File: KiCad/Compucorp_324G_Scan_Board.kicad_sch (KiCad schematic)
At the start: 13 parts, among them J1 Panaplex, J2 Power In, U1 BR 16252

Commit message: Updated keyboard schematic
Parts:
- added J4: From Keyboard, symbol Connector_Generic:Conn_01x28
- J1: value Panaplex -> BR 16252
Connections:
- net A_{10} is gone; now on net Digit_{10}: J1.18 (Pin_18)
- net A_{11} is gone; now on net Digit_{11}: J1.16 (Pin_16)
- net A_{12} is gone; now on net Digit_{12}: J1.14 (Pin_14)
- net A_{13} is gone; now on net Digit_{13}: J1.12 (Pin_12), R14.1, R9.1
- net A_{14} is gone; now on net Digit_{14}: J1.10 (Pin_10)
- net A_{15} is gone; now on net Digit_{15}: J1.4 (Pin_4)
- net A_{16} is gone; now on net Digit_{16}: J1.2 (Pin_2)
- net A_{1} is gone; now on net Digit_{1}: J1.39 (Pin_39)
- net A_{2} is gone; now on net Digit_{2}: J1.37 (Pin_37)
- net A_{3} is gone; now on net Digit_{3}: J1.35 (Pin_35)
- net A_{4} is gone; now on net Digit_{4}: J1.25 (Pin_25)
- net A_{5} is gone; now on net Digit_{5}: J1.24 (Pin_24)
- net A_{6} is gone; now on net Digit_{6}: J1.23 (Pin_23)
- net A_{7} is gone; now on net Digit_{7}: J1.21 (Pin_21)
- net A_{8} is gone; now on net Digit_{8}: J1.20 (Pin_20)
- net A_{9} is gone; now on net Digit_{9}: J1.19 (Pin_19)
- net K_{a}: now also U1.1 (Cathode_{a})
- net K_{b}: now also U1.3 (Cathode_{b})
- net K_{c}: now also U1.5 (Cathode_{c})
- net K_{d}: now also U1.27 (Cathode_{d})
- net K_{e}: now also U1.29 (Cathode_{e})
- net K_{f}: now also U1.33 (Cathode_{f})
- net K_{g}: now also U1.31 (Cathode_{g})
- net K_{h}: now also U1.7 (Cathode_{h})
- net K_{i}: now also U1.11 (Cathode_{j}), U1.9 (Cathode_{i})
- net Digit_{12}: now reaches U1.10 (Anode_{12})
- net Digit_{11}: now reaches U1.12 (Anode_{11})
- net Digit_{10}: now reaches U1.14 (Anode_{10})
- net Digit_{9}: now reaches U1.16 (Anode_{9})
- net Digit_{8}: now reaches U1.18 (Anode_{8})
- net Digit_{16}: now reaches U1.2 (Anode_{16})
- net Digit_{7}: now reaches U1.20 (Anode_{7})
- net Digit_{6}: now reaches U1.22 (Anode_{6})
- net Digit_{5}: now reaches U1.24 (Anode_{5})
- net Digit_{4}: now reaches U1.26 (Anode_{4})
- net Digit_{3}: now reaches U1.28 (Anode_{3})
- net Digit_{2}: now reaches U1.30 (Anode_{2})
- net Digit_{1}: now reaches U1.32 (Anode_{1})
- net Digit_{15}: now reaches U1.4 (Anode_{15})
- net Digit_{14}: now reaches U1.6 (Anode_{14})
- net Digit_{13}: now reaches U1.8 (Anode_{13})
- new net KB Col 1: J4.7 (Pin_7)
- new net KB Col 2: J4.12 (Pin_12)
- new net KB Col 3: J4.8 (Pin_8)
- new net KB Col 4: J4.11 (Pin_11)
- new net KB Col 5: J4.9 (Pin_9)
- new net KB Col 6: J4.13 (Pin_13)
- new net KB Col 7: J4.16 (Pin_16)
- new net KB Col 8: J4.17 (Pin_17)
- new net KB Col 9: J4.18 (Pin_18)
- new net KB FED: J4.21 (Pin_21)
- new net KB GRAD: J4.24 (Pin_24)
- new net KB LOAD: J4.22 (Pin_22)
- new net KB PROG 1: J4.6 (Pin_6)
- new net KB RUN: J4.23 (Pin_23), J4.5 (Pin_5)
- new net KB Row 1: J4.1 (Pin_1)
- new net KB Row 2: J4.2 (Pin_2)
- new net KB Row 3: J4.3 (Pin_3)
- new net KB Row 4: J4.4 (Pin_4)
- new net KB Row 5: J4.25 (Pin_25)
- new net KB Row 6: J4.26 (Pin_26)
- new net KB Row 7: J4.27 (Pin_27)
- new net KB Row 8: J4.28 (Pin_28)
- new net TCL02 Pin 38: J4.20 (Pin_20)
- no-connect marks 14 -> 18
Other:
- moved on the sheet: J1, R10, R7, R8, R9, U1

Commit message: Update Compucorp_324G_Scan_Board.kicad_sch
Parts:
- added D1, D2, D3, D4, D5, D6, D7, D8: D, symbol Device:D
- added U4: TMC 1869, symbol Clueless_Engineer:TMC_1869
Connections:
- net KB Col 7: now also U4.33 (Pin_33)
- net KB Col 8: now also U4.34 (Pin_34)
- net KB Col 9: now also U4.35 (Pin_35)
- net KB FED: now also D1.2 (A)
- net KB GRAD: now also D5.2 (A)
- net KB LOAD: now also D3.2 (A)
- net KB Row 5: now also D2.2 (A)
- net KB Row 6: now also D4.2 (A)
- net KB Row 8: now also D8.2 (A)
- net TCL02 Pin 38: now also U4.38 (Pin_38)
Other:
- moved on the sheet: U2, U3

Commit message: Updates to schematic
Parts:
- removed J1: BR 16252, symbol Connector_Generic:Conn_01x40
- removed U1: BR 16252, symbol Clueless_Engineer:Panaplex II 16dig
- removed U2, U3: ~, symbol Clueless_Engineer:UHP480
- removed U4: TMC 1869, symbol Clueless_Engineer:TMC_1869
- added J1: Scan Interboard, symbol Connector_Generic:Conn_02x40_Row_Letter_First
- added U1: BR 16252, symbol Compucorp_324G_Scientist:Panaplex II 16dig
- added U2, U3: UHP480, symbol Compucorp_324G_Scientist:UHP480
- added U4: TMC 1869, symbol Compucorp_324G_Scientist:TMC_1869
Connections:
- net Digit_{10}: now also J1.a18 (Pin_a18), U1.14 (Anode_{10})
- net Digit_{11}: now also J1.a16 (Pin_a16), U1.12 (Anode_{11})
- net Digit_{12}: now also J1.a14 (Pin_a14), U1.10 (Anode_{12})
- net Digit_{13}: now also J1.a12 (Pin_a12), U1.8 (Anode_{13})
- net Digit_{14}: now also J1.a10 (Pin_a10), U1.6 (Anode_{14})
- net Digit_{15}: now also J1.a4 (Pin_a4), U1.4 (Anode_{15})
- net Digit_{16}: now also J1.a2 (Pin_a2), U1.2 (Anode_{16})
- net Digit_{1}: now also J1.a39 (Pin_a39), U1.32 (Anode_{1})
- net Digit_{2}: now also J1.a37 (Pin_a37), U1.30 (Anode_{2})
- net Digit_{3}: now also J1.a35 (Pin_a35), U1.28 (Anode_{3})
- net Digit_{4}: now also J1.a25 (Pin_a25), U1.26 (Anode_{4})
- net Digit_{5}: now also J1.a24 (Pin_a24), U1.24 (Anode_{5})
- net Digit_{6}: now also J1.a23 (Pin_a23), U1.22 (Anode_{6})
- net Digit_{7}: now also J1.a21 (Pin_a21), U1.20 (Anode_{7})
- net Digit_{8}: now also J1.a20 (Pin_a20), U1.18 (Anode_{8})
- net Digit_{9}: now also J1.a19 (Pin_a19), U1.16 (Anode_{9})
- net KB Col 7: now also U4.33 (Pin_33)
- net KB Col 8: now also U4.34 (Pin_34)
- net KB Col 9: now also U4.35 (Pin_35)
- net K_{a}: now also J1.a1 (Pin_a1), U1.1 (Cathode_{a})
- net K_{b}: now also J1.a3 (Pin_a3), U1.3 (Cathode_{b})
- net K_{c}: now also J1.a9 (Pin_a9), U1.5 (Cathode_{c})
- net K_{d}: now also J1.a26 (Pin_a26), U1.27 (Cathode_{d})
- net K_{e}: now also J1.a36 (Pin_a36), U1.29 (Cathode_{e})
- net K_{f}: now also J1.a40 (Pin_a40), U1.33 (Cathode_{f})
- net K_{g}: now also J1.a38 (Pin_a38), U1.31 (Cathode_{g})
- net K_{h}: now also J1.a11 (Pin_a11), U1.7 (Cathode_{h})
- net K_{i}: now also J1.a13 (Pin_a13), J1.a15 (Pin_a15), U1.11 (Cathode_{j}), U1.9 (Cathode_{i})
- net U2_Pin9: now also U2.9 (Pin9)
- net U3_Pin9: now also U3.9 (Pin9)
- net TCL02 Pin 38 renamed TCL02_38
- net TCL02_38: now also U4.38 (Pin_38)

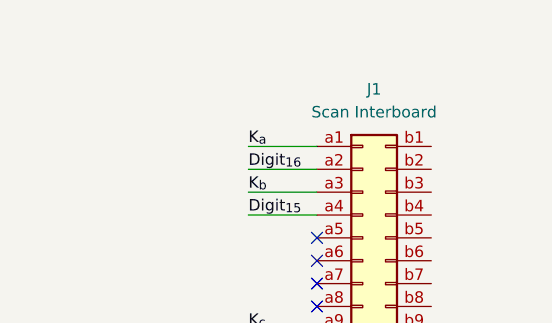
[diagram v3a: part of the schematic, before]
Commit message: Started on other board schematics
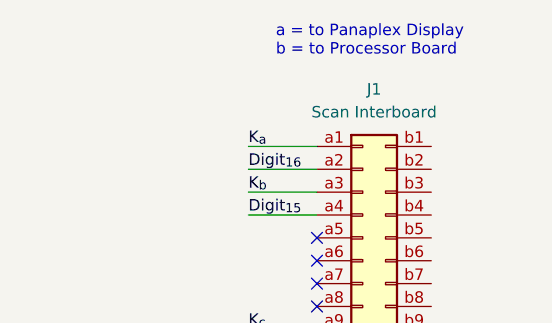
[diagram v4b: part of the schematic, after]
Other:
- note added: "a = to Panaplex Display b = to Processor Board"
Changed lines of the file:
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@@
 		(company "Brett Hallen")
+	)
+	(text "a = to Panaplex Display\nb = to Processor Board"
+		(exclude_from_sim no)
+		(at 246.888 23.876 0)
+		(effects
+			(font
+				(size 1.27 1.27)
+			)
+			(justify left)
+		)
 	)
 	(junction

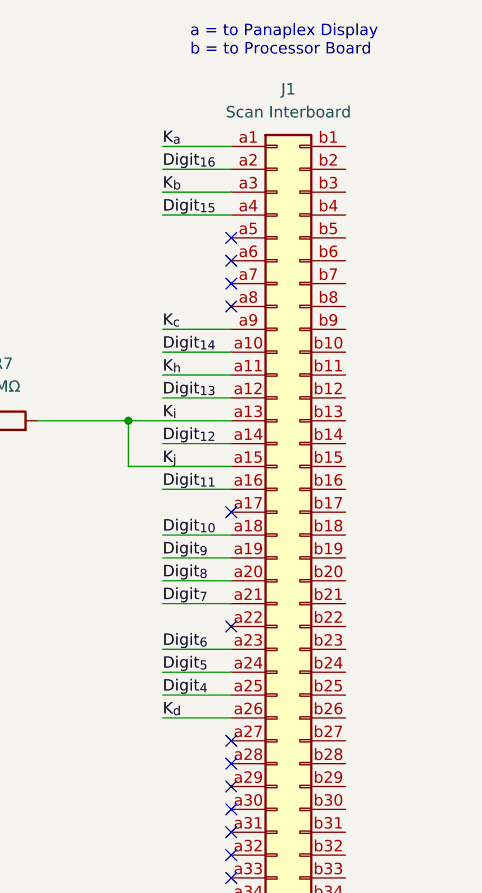
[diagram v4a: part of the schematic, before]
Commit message: Started Memory Board schematic
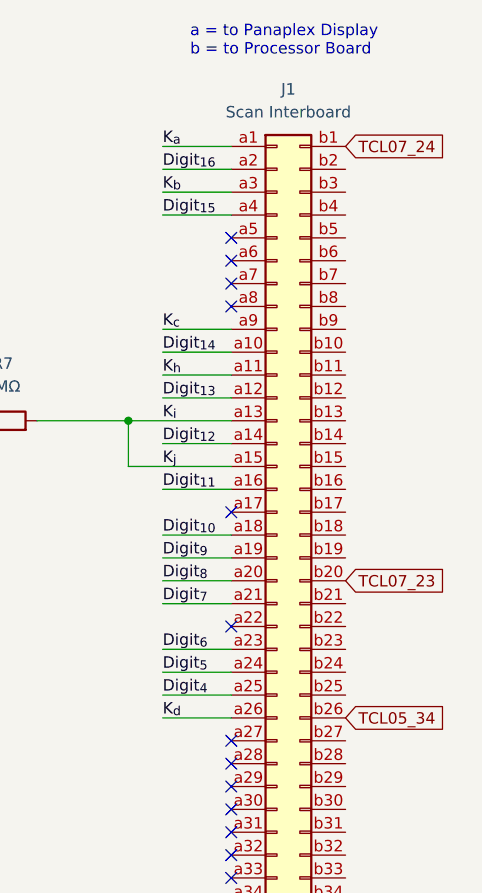
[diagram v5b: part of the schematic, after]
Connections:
- net TCL07_24: now reaches J1.b1 (Pin_b1)
- net TCL07_23: now reaches J1.b20 (Pin_b20)
- net TCL05_34: now reaches J1.b26 (Pin_b26)
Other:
- title: Compucorp 320-Series Scan Board -> Compucorp 300-Series Scan Board
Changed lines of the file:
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@@
 	(generator "eeschema")
 	(generator_version "9.0")
-	(paper "A4")
+	(paper "A3")
 	(title_block
-		(title "Compucorp 320-Series Scan Board")
+		(title "Compucorp 300-Series Scan Board")
 		(rev "WIP")
 		(company "Brett Hallen")
@@
 		)
 	)
+	(global_label "TCL07_23"
+		(shape input)
+		(at 264.16 83.82 0)
+		(fields_autoplaced yes)
+		(effects
+			(font
+				(size 1.27 1.27)
+			)
+			(justify left)
+		)
+		(property "Intersheetrefs" "${INTERSHEET_REFS}"
+			(at 276.2165 83.82 0)
+			(effects
+				(font
+					(size 1.27 1.27)
+				)
+				(justify left)
+				(hide yes)
+			)
+		)
+	)
 	(global_label "KB LOAD"
 		(shape input)
@@
 		)
 	)
+	(global_label "TCL05_34"
+		(shape input)
+		(at 264.16 99.06 0)
+		(fields_autoplaced yes)
+		(effects
+			(font
+				(size 1.27 1.27)
+			)
+			(justify left)
+		)
+		(property "Intersheetrefs" "${INTERSHEET_REFS}"
+			(at 276.2165 99.06 0)
+			(effects
+				(font
+					(size 1.27 1.27)
+				)
+				(justify left)
+				(hide yes)
+			)
+		)
+	)
 	(global_label "KB RUN"
 		(shape input)
@@
 				(hide yes)
 			)
+		)
+	)
+	(global_label "TCL07_24"
+		(shape input)
+		(at 264.16 35.56 0)
+		(fields_autoplaced yes)
+		(effects
+			(font
+				(size 1.27 1.27)
+			)
+			(justify left)
+		)
+		(property "Intersheetrefs" "${INTERSHEET_REFS}"
+			(at 276.2165 35.56 0)
+			(effects
+				(font
+					(size 1.27 1.27)
+				)
+				(justify left)
+				(hide yes)
+			)

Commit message: Memory board updates
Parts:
- removed U4: TMC 1869, symbol Compucorp_324G_Scientist:TMC_1869
- added U4: TMC1869 (TCL02), symbol Compucorp_324G_Scientist:TMC1869
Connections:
- net KB Col 7: now also U4.33 (Pin_33)
- net KB Col 8: now also U4.34 (Pin_34)
- net KB Col 9: now also U4.35 (Pin_35)
- net TCL02_38: now also U4.38 (Pin_38)

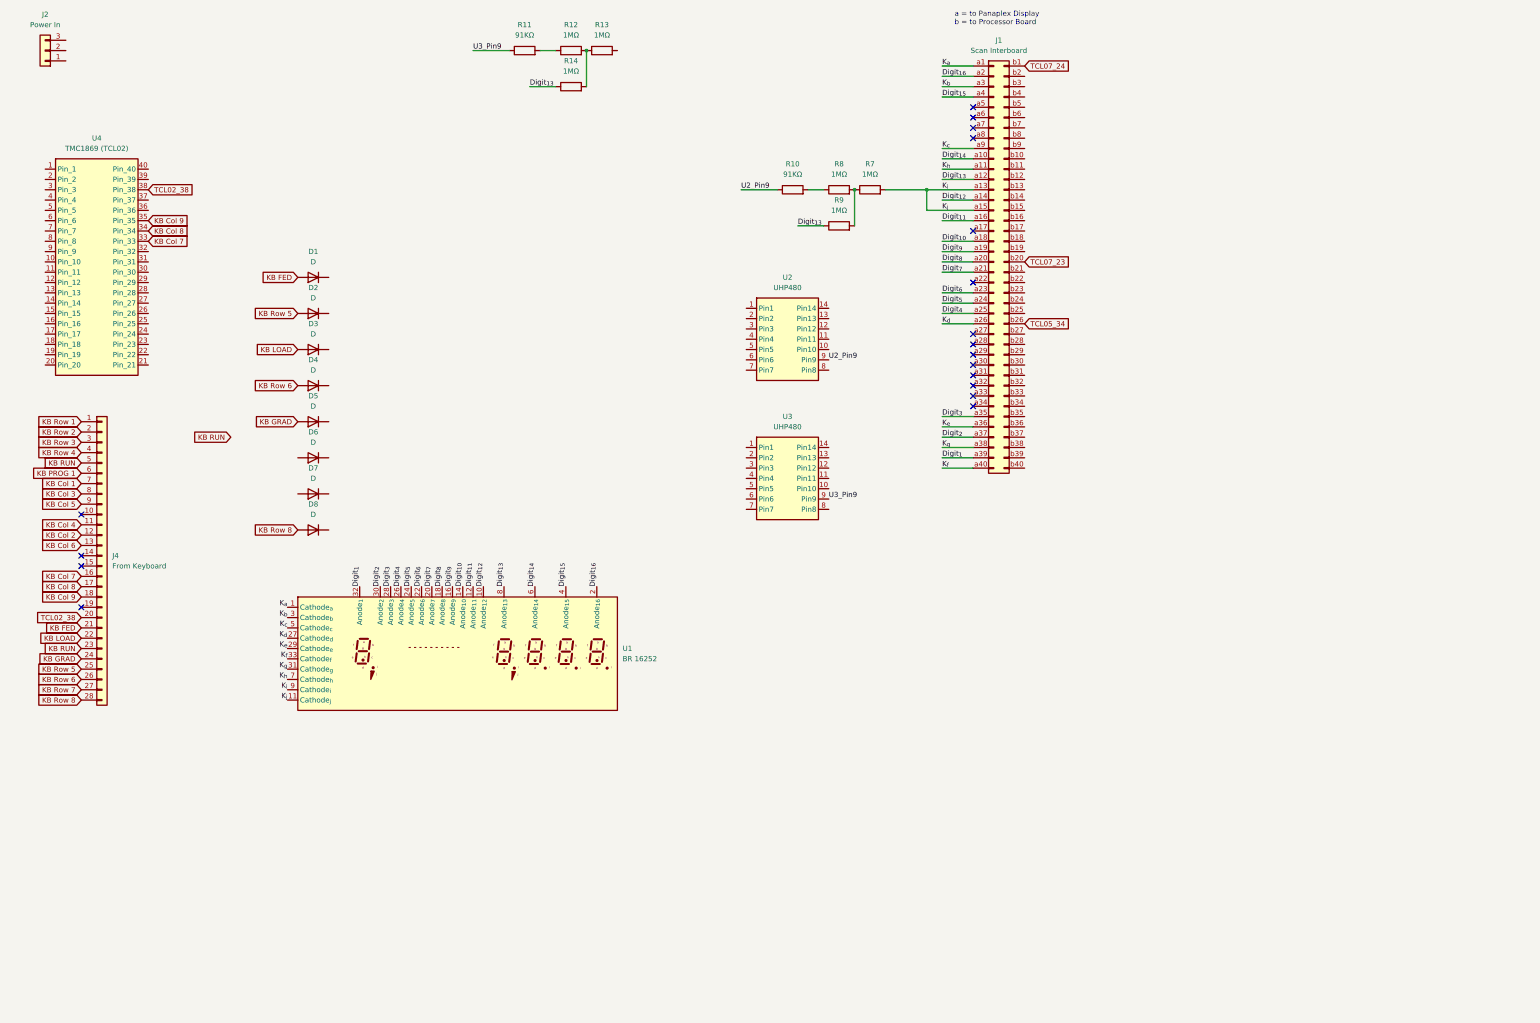
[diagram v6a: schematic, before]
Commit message: Schematic updates
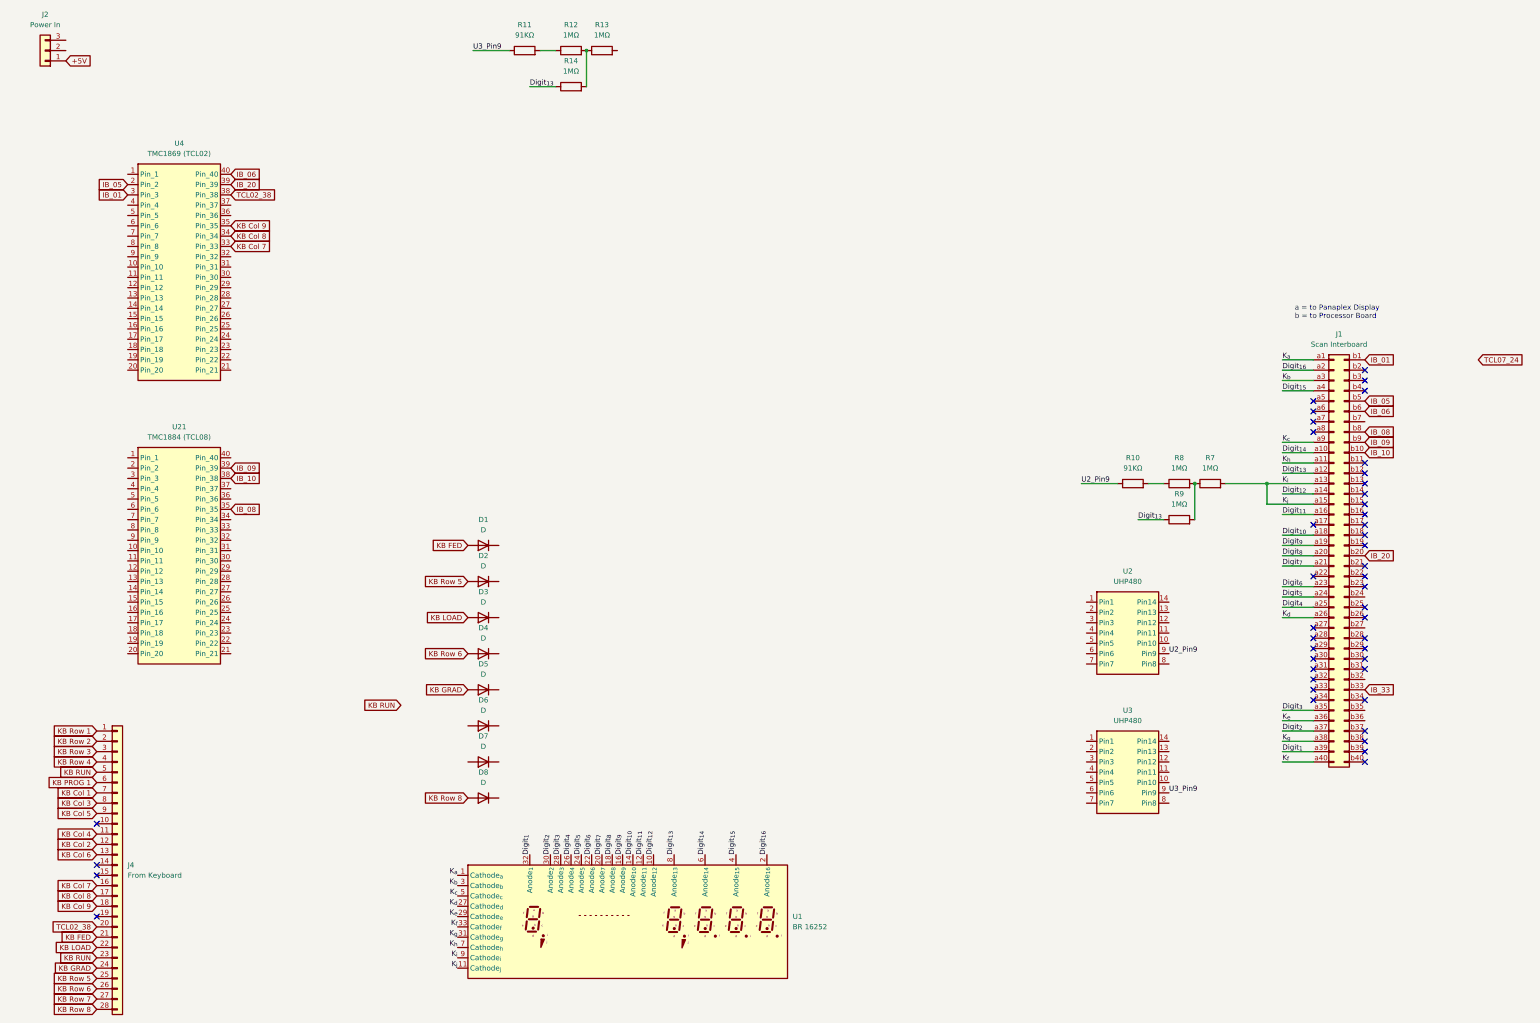
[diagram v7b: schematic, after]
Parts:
- added U21: TMC1884 (TCL08), symbol Compucorp_324G_Scientist:TMC1884
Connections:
- net TCL07_23 is gone; now on net IB_20: J1.b20 (Pin_b20)
- net TCL07_24: no longer J1.b1 (Pin_b1)
- net +5V: now reaches J2.1 (Pin_1)
- net IB_05: now reaches U4.2 (Pin_2)
- net IB_05: now also J1.b5 (Pin_b5)
- net IB_01: now reaches U4.3 (Pin_3)
- net IB_01: now also J1.b1 (Pin_b1)
- net IB_20: now reaches U4.39 (Pin_39)
- net IB_06: now reaches U4.40 (Pin_40)
- net IB_06: now also J1.b6 (Pin_b6)
- net IB_10: now reaches J1.b10 (Pin_b10)
- net IB_10: now also U21.38 (Pin_38)
- net IB_33: now reaches J1.b33 (Pin_b33)
- net IB_08: now reaches J1.b8 (Pin_b8)
- net IB_08: now also U21.35 (Pin_35)
- net IB_09: now reaches J1.b9 (Pin_b9)
- net IB_09: now also U21.39 (Pin_39)
- net TCL05_34: no longer names the net of J1.b26 (Pin_b26)
- no-connect marks 18 -> 44
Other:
- moved on the sheet: D1, D2, D3, D4, D5, D6, D7, D8, J1, J4, R10, R7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
